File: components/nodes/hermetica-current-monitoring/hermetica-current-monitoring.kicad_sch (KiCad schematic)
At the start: 4 parts, among them U1 INA238

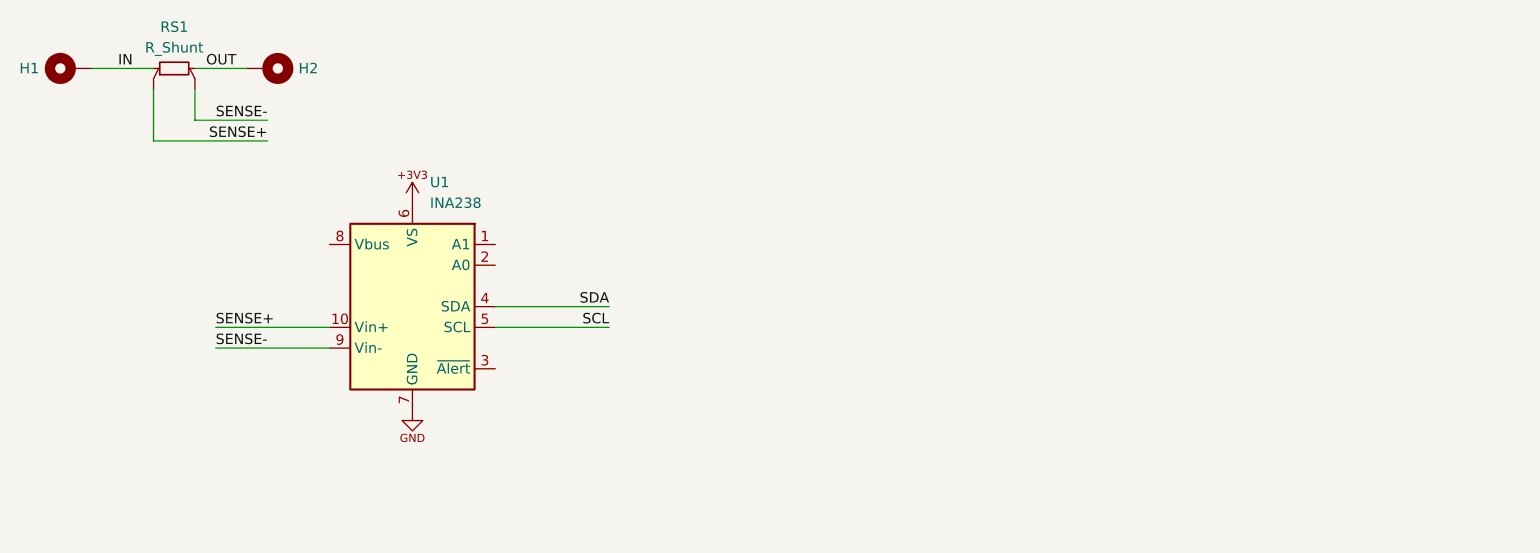
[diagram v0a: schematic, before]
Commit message: Primarily added monitoring tool
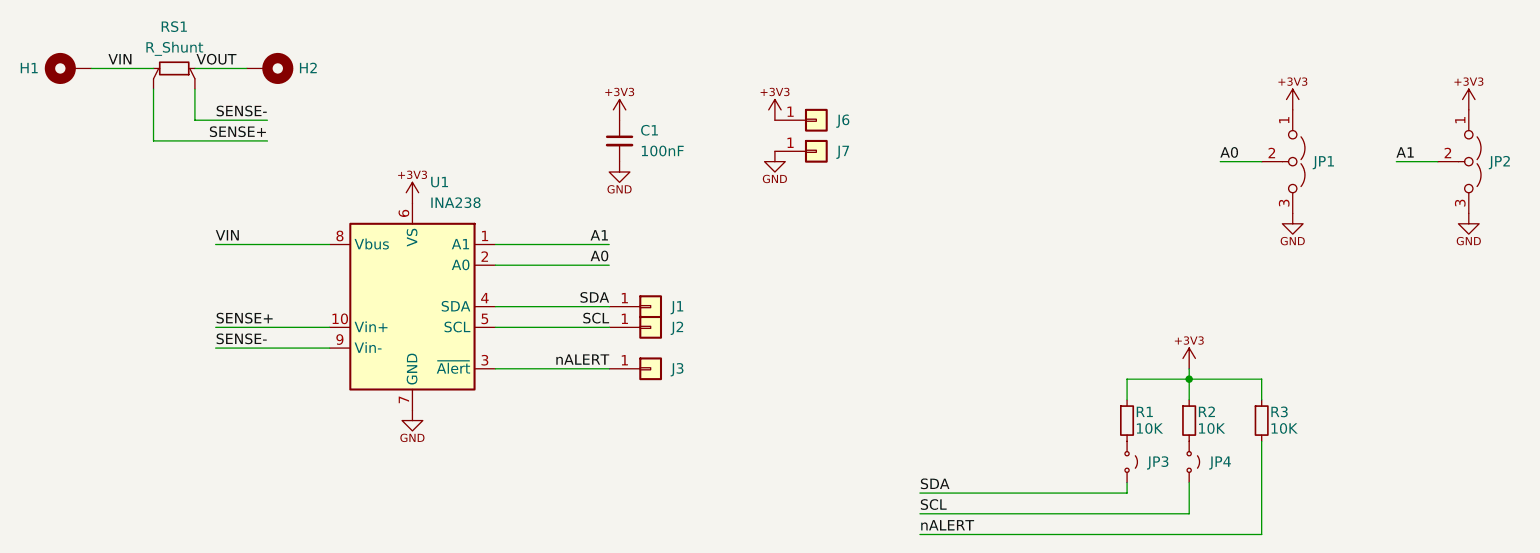
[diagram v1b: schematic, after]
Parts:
- added C1: 100nF, djStandard:C_0603_1608Metric, symbol DJ:C
- added J1, J2, J3, J6, J7: Conn_01x01, djStandard:CONNECTOR-PCB-HANDSOLDER-01X01, symbol Connector_Generic:Conn_01x01
- added JP1, JP2: Jumper_3_Open, djStandard:SolderJumper-3_P1.3mm_Bridged12_RoundedPad1.0x1.5mm, symbol Jumper:Jumper_3_Open
- added JP3, JP4: Jumper_2_Small_Open, djStandard:SolderJumper-2_P1.3mm_Bridged_RoundedPad1.0x1.5mm, symbol Jumper:Jumper_2_Small_Open
- added R1, R2, R3: 10K, djStandard:R_0402_1005Metric, symbol DJ:R
- H1, H2: footprint djStandard:MountingHole_M4.0_AWG10_SmallPad -> djStandard:MountingHole_M2.5_AWG14_SmallPad
- RS1: footprint djStandard:OHMITE-FC4L64-2512 -> djStandard:VISHAY-WSL27261L300FEA
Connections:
- net +3V3: now also C1.1, J6.1 (Pin_1), JP1.1 (A), JP2.1 (A), R1.1, R2.1, R3.1
- net GND: now also C1.2, J7.1 (Pin_1), JP1.3 (B), JP2.3 (B)
- net SCL: now also J2.1 (Pin_1), JP4.2 (B)
- net SDA: now also J1.1 (Pin_1), JP3.2 (B)
- net SENSE+: now also RS1.4; no longer RS1.3
- net SENSE-: now also RS1.3; no longer RS1.4
- net A1: now reaches U1.1 (A1)
- net A1: now also JP2.2 (C)
- net A0: now reaches U1.2 (A0)
- net A0: now also JP1.2 (C)
- net nALERT: now reaches U1.3 (~{Alert})
- net nALERT: now also J3.1 (Pin_1), R3.2
- net VIN: now reaches U1.8 (Vbus)
- net VIN: now also H1.1, RS1.2
- net IN renamed VOUT
- net VOUT: now also H2.1; no longer H1.1
- removed net OUT: H2.1, RS1.2
- new net: JP4.1 (A), R2.2
- new net: JP3.1 (A), R1.2
